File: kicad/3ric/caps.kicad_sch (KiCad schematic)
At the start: 25 parts

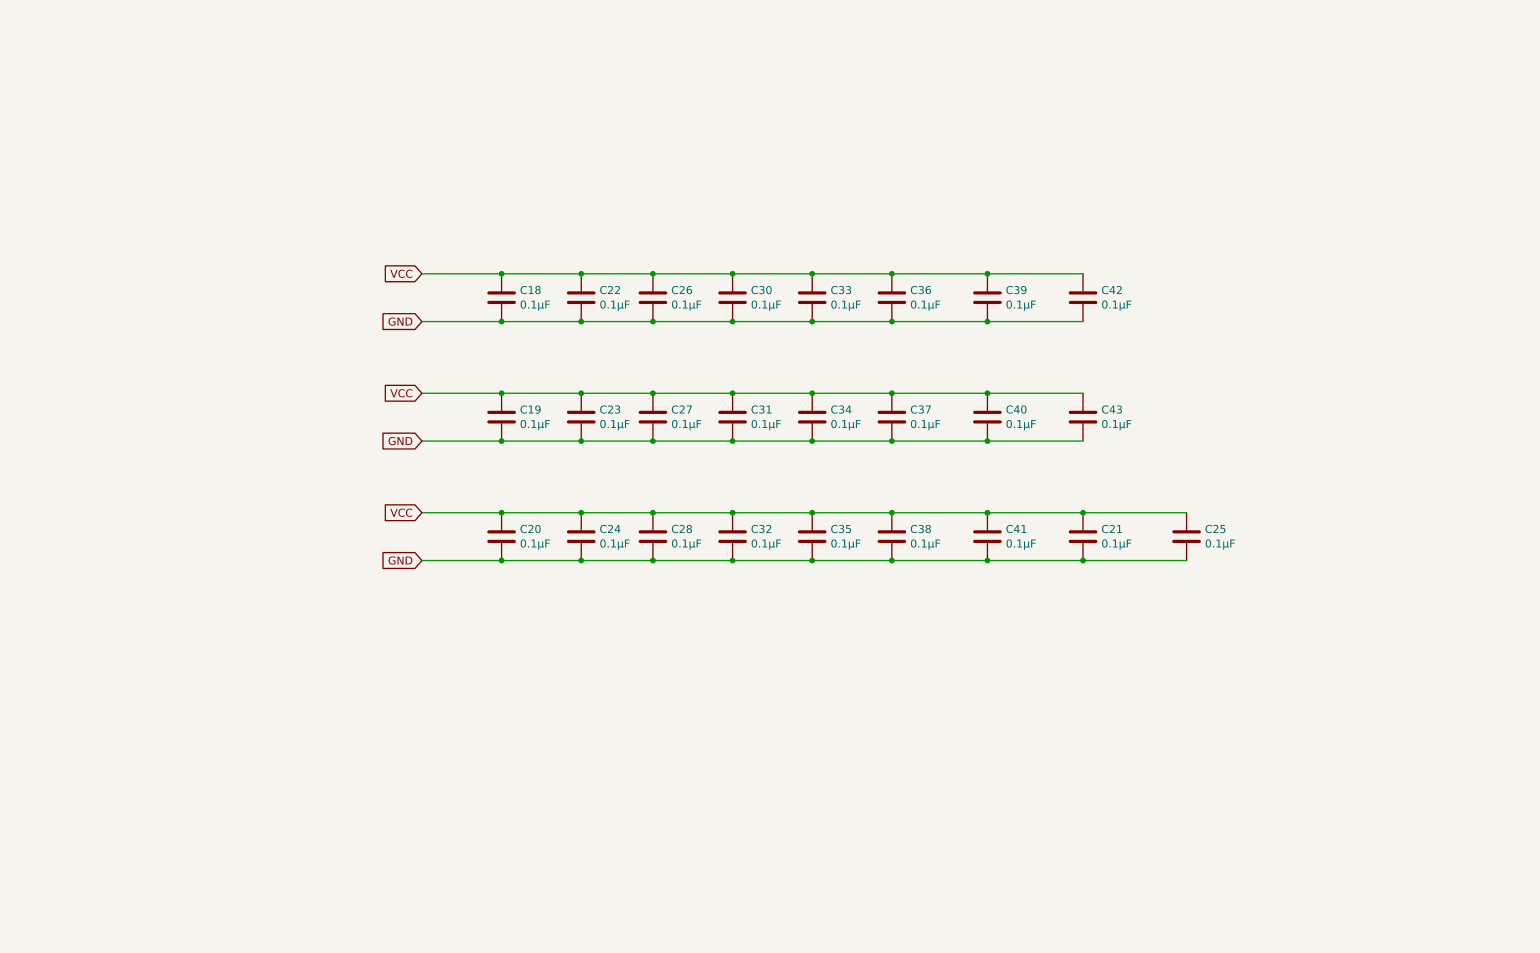
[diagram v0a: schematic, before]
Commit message: schematic updates - bring the schematics up to match breadboard changes current state has high res Apple II color emulation working
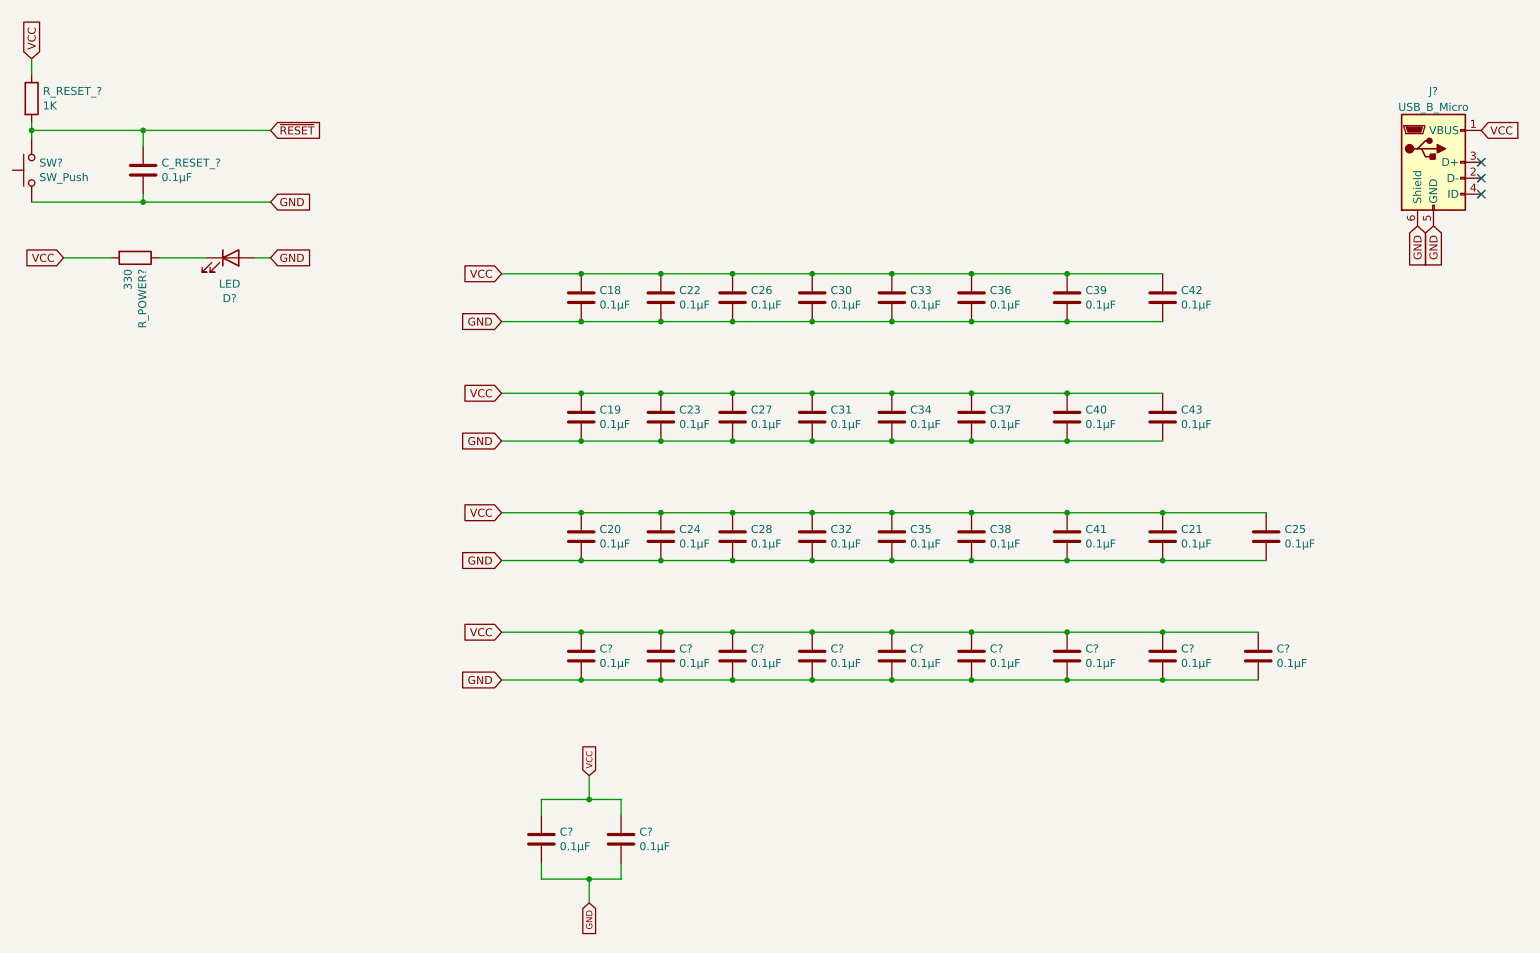
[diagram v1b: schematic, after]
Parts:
- added C? (x11), C_RESET_?: 0.1µF, Capacitor_THT:C_Axial_L3.8mm_D2.6mm_P7.50mm_Horizontal, symbol Device:C
- added D?: LED, LED_THT:LED_D5.0mm, symbol Device:LED
- added J?: USB_B_Micro, Connector_USB:USB_Micro-B_Molex-105017-0001, symbol Connector:USB_B_Micro
- added R_POWER?: 330, Resistor_THT:R_Axial_DIN0207_L6.3mm_D2.5mm_P7.62mm_Horizontal, symbol Device:R
- added R_RESET_?: 1K, Resistor_THT:R_Axial_DIN0207_L6.3mm_D2.5mm_P7.62mm_Horizontal, symbol Device:R
- added SW?: SW_Push, Button_Switch_THT:SW_PUSH_6mm, symbol Switch:SW_Push
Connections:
- net GND: now also C?.2, C?.2, C?.2, C?.2, C?.2, C?.2, C?.2, C?.2, C?.2, C?.2, C?.2, C_RESET_?.2, D?.2 (A), J?.5 (GND), J?.6 (Shield), SW?.1
- net VCC: now also C?.1, C?.1, C?.1, C?.1, C?.1, C?.1, C?.1, C?.1, C?.1, C?.1, C?.1, J?.1 (VBUS), R_POWER?.2, R_RESET_?.1
- new net: D?.1 (K), R_POWER?.1
- new net ~{RESET}: C_RESET_?.1, R_RESET_?.2, SW?.2
- no-connect marks 0 -> 3
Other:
- moved on the sheet: C18, C19, C20, C21, C22, C23, C24, C25, C26, C27, C28, C30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
